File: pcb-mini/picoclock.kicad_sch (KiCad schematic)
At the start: 83 parts, among them J1 UART, J10 USB, J11 Alt Power, J12 LED_5V, J14 SJ2-35863B1-SMT-TR, J2 USB_A, J3 UART, J4 xx, J5 Micro_SD_Card_Det1, J6 USB_C_Receptacle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

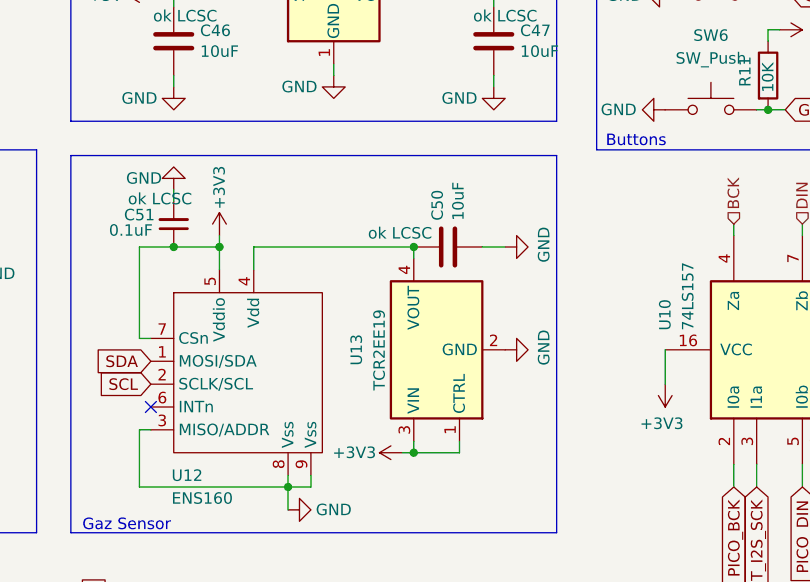
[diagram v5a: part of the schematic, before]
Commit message: [pcb] mini: tweaks
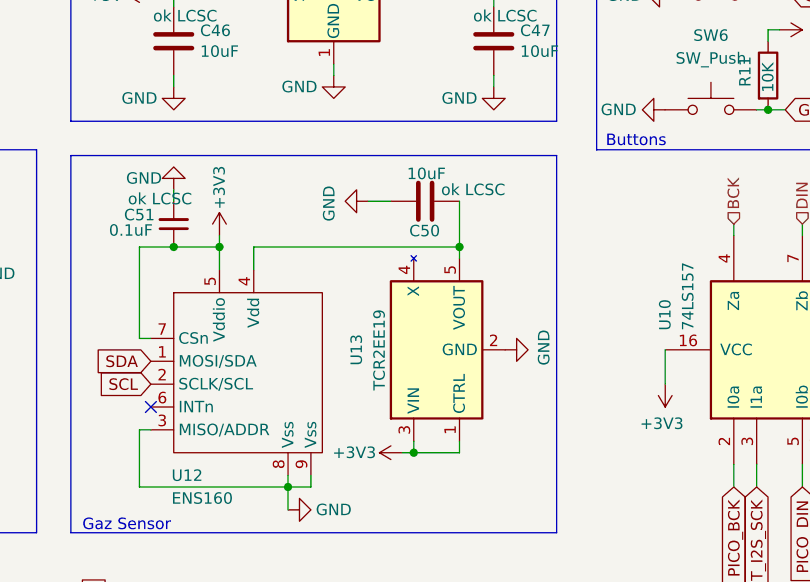
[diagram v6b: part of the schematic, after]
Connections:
- net at C50.1, U12.4 (Vdd): now also U13.5 (VOUT); no longer U13.4 (VOUT)
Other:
- moved on the sheet: C50
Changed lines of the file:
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@@
 	)
 	(junction
+		(at 119.38 107.95)
+		(diameter 0)
+		(color 0 0 0 0)
+	)
+	(junction
 		(at 150.495 189.23)
 		(diameter 0)
@@
 		(color 0 0 0 0)
 	)
-	(junction
-		(at 114.3 107.95)
-		(diameter 0)
-		(color 0 0 0 0)
-	)
 	(no_connect
 		(at 233.68 121.92)
@@
 	(wire
 		(pts
-			(xy 114.3 107.95) (xy 114.3 109.22)
-		)
-		(stroke
-			(width 0)
-			(type default)
-		)
-	)
-	(wire
-		(pts
 			(xy 138.43 34.29) (xy 138.43 35.56)
 		)
@@
 	(wire
 		(pts
-			(xy 124.46 107.95) (xy 121.92 107.95)
+			(xy 109.22 102.87) (xy 111.76 102.87)
 		)
 		(stroke
@@
 	(wire
 		(pts
+			(xy 119.38 102.87) (xy 119.38 107.95)
+		)
+		(stroke
+			(width 0)
+			(type default)
+		)
+	)
+	(wire
+		(pts
 			(xy 232.41 31.75) (xy 232.41 26.67)
 		)
@@
 	(wire
 		(pts
-			(xy 96.52 107.95) (xy 114.3 107.95)
+			(xy 96.52 107.95) (xy 119.38 107.95)
 		)
 		(stroke
@@
 	(wire
 		(pts
+			(xy 119.38 107.95) (xy 119.38 109.22)
+		)
+		(stroke
+			(width 0)
+			(type default)
+		)
+	)
+	(wire
+		(pts
 			(xy 149.86 166.37) (xy 153.67 166.37)
 		)
@@
 	(symbol
 		(lib_id "Device:C")
-		(at 118.11 107.95 90)
+		(at 115.57 102.87 270)
 		(unit 1)
 		(exclude_from_sim no)
@@
 		(dnp no)
 		(property "Reference" "C50"
-			(at 116.9416 105.029 0)
+			(at 113.792 106.172 90)
 			(effects
 				(font
@@
 		)
 		(property "Value" "10uF"
-			(at 119.253 105.029 0)
+			(at 113.538 99.822 90)
 			(effects
 				(font
@@
 		)
 		(property "Footprint" "Capacitor_SMD:C_0805_2012Metric"
-			(at 121.92 106.9848 0)
+			(at 111.76 103.8352 0)
 			(effects
 				(font
@@
 		)
 		(property "Datasheet" "~"
-			(at 118.11 107.95 0)
+			(at 115.57 102.87 0)
 			(effects
 				(font
@@
 		)
 		(property "Description" "ok LCSC"
-			(at 112.776 106.426 90)
+			(at 120.904 101.6 90)
 			(effects
 				(font
@@
 		)
 		(property "LCSC" "C15850"
-			(at 118.11 107.95 0)
+			(at 115.57 102.87 0)
 			(effects
 				(font
@@
 	(symbol
 		(lib_id "power:GND")
-		(at 124.46 107.95 90)
+		(at 109.22 102.87 270)
 		(unit 1)
 		(exclude_from_sim no)
@@
 		(dnp no)
 		(property "Reference" "#PWR0113"
-			(at 130.81 107.95 0)
+			(at 102.87 102.87 0)
 			(effects
 				(font
@@
 		)
 		(property "Value" "GND"
-			(at 128.778 107.696 0)
+			(at 104.902 103.124 0)
 			(effects
 				(font
@@
 		)
 		(property "Footprint" ""
-			(at 124.46 107.95 0)
+			(at 109.22 102.87 0)
 			(effects
 				(font
@@
 		)
 		(property "Datasheet" ""
-			(at 124.46 107.95 0)
+			(at 109.22 102.87 0)
 			(effects
 				(font
@@
 		)
 		(property "Description" ""
-			(at 124.46 107.95 0)
+			(at 109.22 102.87 0)
 			(effects
 				(font

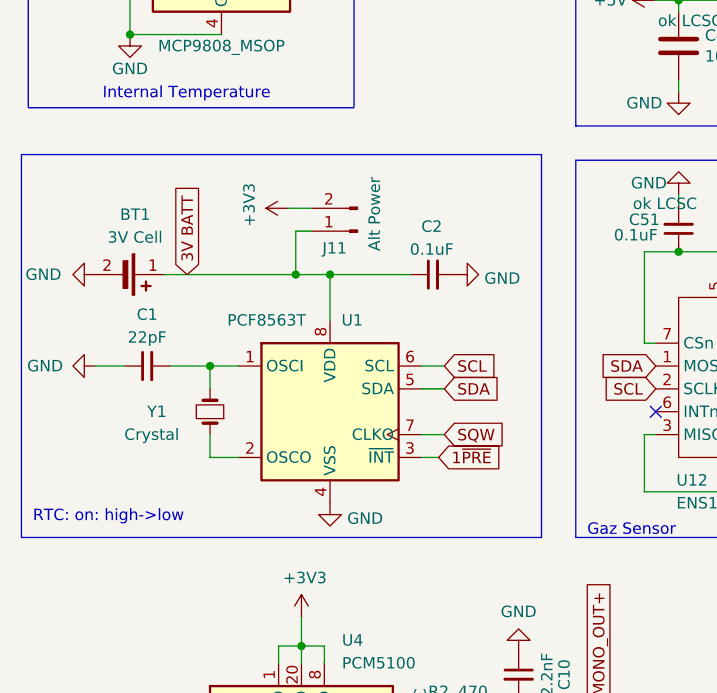
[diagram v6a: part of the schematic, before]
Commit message: [pcb] mini: RTC: add diods, wire INT. fix 74LS chip footprint
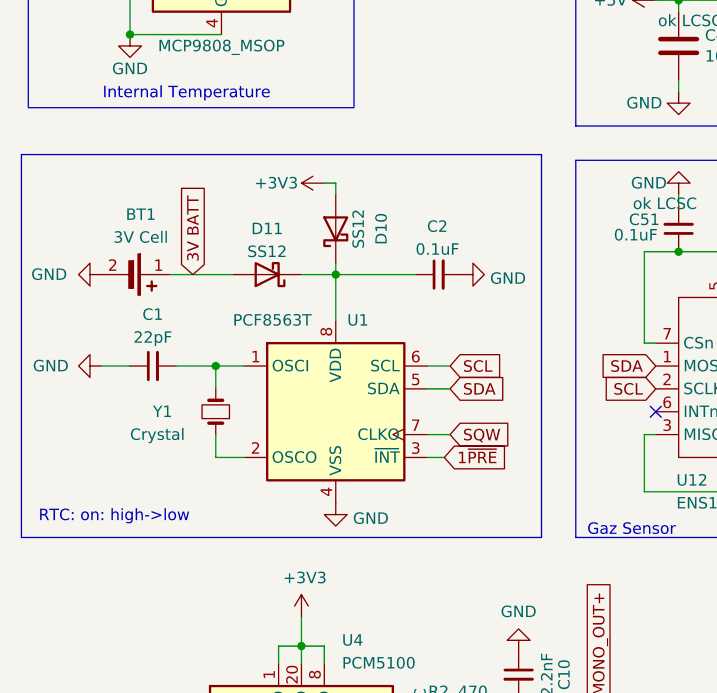
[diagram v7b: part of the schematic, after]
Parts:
- removed J11: Alt Power, Connector_PinHeader_2.54mm:PinHeader_1x02_P2.54mm_Vertical, symbol Connector:Conn_01x02_Pin
- added D10, D11: SS12, Diode_SMD:D_SOD-323, symbol Diode:SS12
- U10: footprint Package_SO:SOIC-16_3.9x9.9mm_P1.27mm -> Package_SO:SOP-16_4.55x10.3mm_P1.27mm
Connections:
- net +3V3: now also D10.2 (A)
- net 3V BATT: now also D11.2 (A); no longer C2.1, U1.8 (VDD)
- new net: C2.1, D10.1 (K), D11.1 (K), U1.8 (VDD)
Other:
- moved on the sheet: BT1, C1, C2, U1, Y1

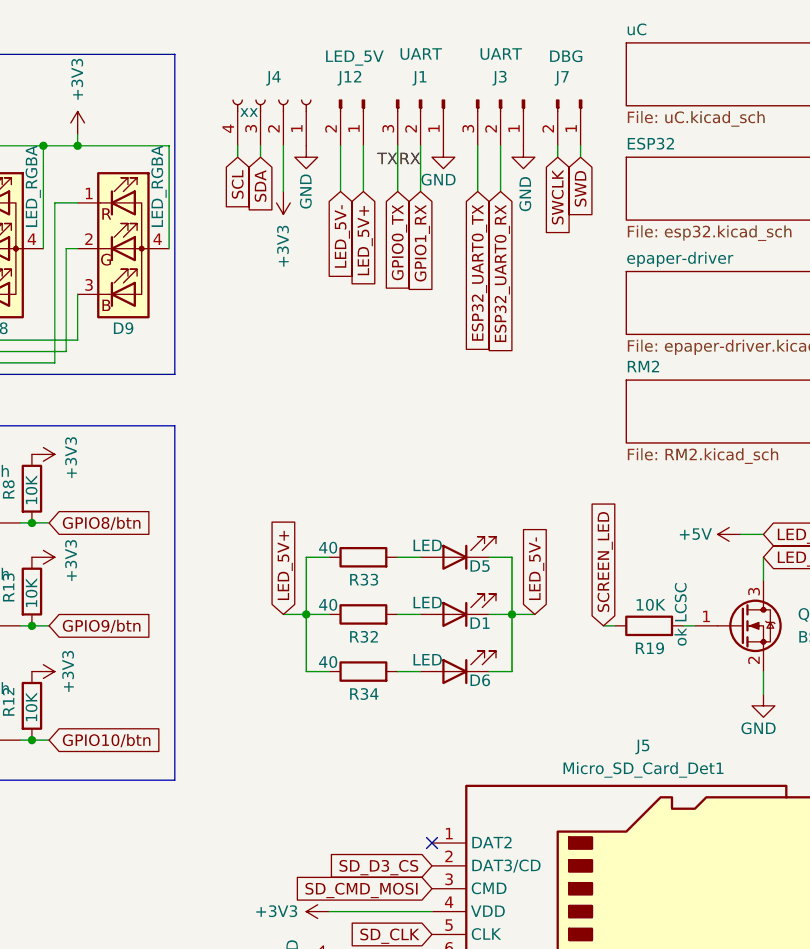
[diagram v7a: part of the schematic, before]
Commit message: [pcb] mini: add senseair schema+footprint
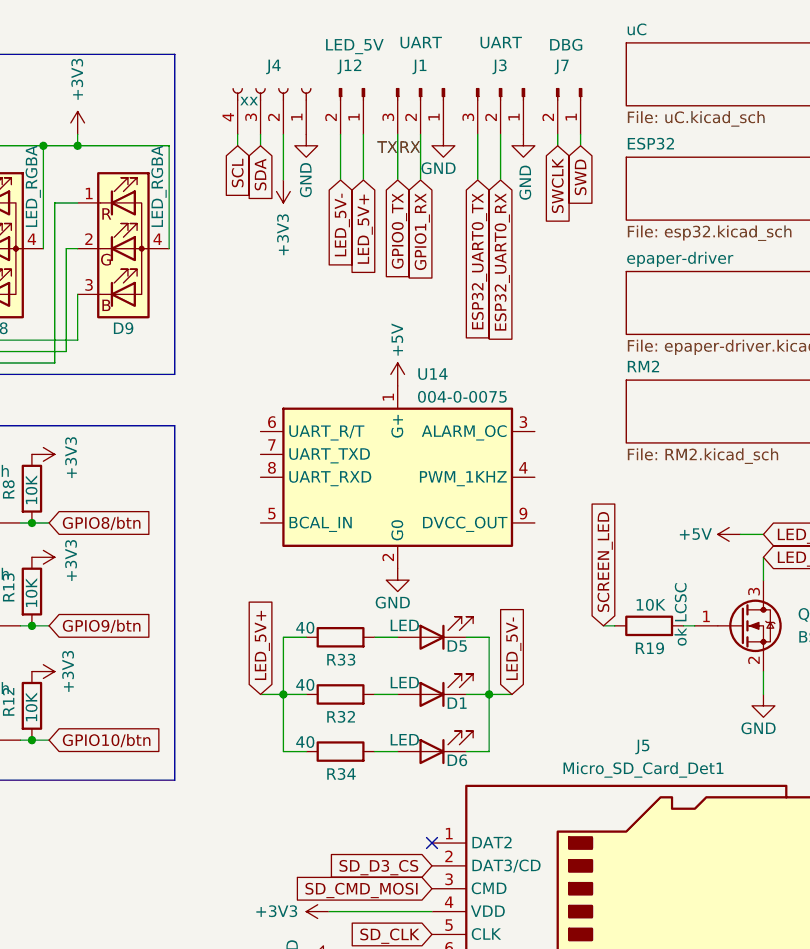
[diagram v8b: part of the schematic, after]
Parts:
- added U14: 004-0-0075, senseair:Senseair_S8_Down, symbol senseair_S8:004-0-0075
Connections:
- net +5V: now also U14.1 (G+)
- net GND: now also U14.2 (G0)
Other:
- moved on the sheet: D1, D5, D6, J1, J12, J3, J4, J7, R32, R33, R34
